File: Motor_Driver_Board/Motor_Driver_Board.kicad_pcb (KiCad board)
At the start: 2 copper layers, 74.5 x 55 mm, 9 parts, among them J1 Conn_01x02_MountingPin, J2 Conn_01x04_MountingPin

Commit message: Shcematic and layout
Updated the schematic.
Updated the layout.
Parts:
- removed REF** (x4): MountingHole_3.5mm, MountingHole:MountingHole_3.5mm
- added C2: 100u, Capacitor_THT:CP_Radial_D6.3mm_P2.50mm, F.Cu at (148.8, 60.6)
- added C3: 10u, Capacitor_SMD:C_1206_3216Metric, F.Cu at (144.3, 60.6)
- added C4: 47u, Capacitor_SMD:C_1206_3216Metric, F.Cu at (132.8, 63.6)
- added C5: 47u, Capacitor_SMD:C_1206_3216Metric, F.Cu at (132.8, 60.6)
- added C6: 47u, Capacitor_SMD:C_1206_3216Metric, F.Cu at (132.8, 57.6)
- added C7: 10n, Capacitor_SMD:C_0603_1608Metric, F.Cu at (188.5, 42.6)
- added C8: 10n, Capacitor_SMD:C_0603_1608Metric, F.Cu at (188.5, 45.1)
- added C9: 10n, Capacitor_SMD:C_0603_1608Metric, F.Cu at (188.5, 47.7)
- added D1: SS34, Diode_SMD:D_SMA, F.Cu at (148.8, 49.6)
- added H1: MH, MountingHole:MountingHole_3.2mm_M3, F.Cu at (67.3, 39.6)
- added H2: MH, MountingHole:MountingHole_3.2mm_M3, F.Cu at (157.3, 39.6)
- added H3: MH, MountingHole:MountingHole_3.2mm_M3, F.Cu at (67.3, 129.6)
- added H4: MH, MountingHole:MountingHole_3.2mm_M3, F.Cu at (157.3, 129.6)
- added J3: LCD, Connector_PinHeader_2.54mm:PinHeader_1x04_P2.54mm_Vertical, F.Cu at (190.3, 77.5)
- added L1: FXL1040-680-M, Inductor_SMD:L_Sunlord_MWSA1005S, F.Cu at (139.3, 49.6)
- added R1: 10K, Resistor_SMD:R_0603_1608Metric, F.Cu at (188.5, 50.2)
- added R10: 10K, Resistor_SMD:R_0603_1608Metric, F.Cu at (194.6, 76.4)
- added R11: 10K, Resistor_SMD:R_0603_1608Metric, F.Cu at (194.6, 79.0)
- added R2: 10K, Resistor_SMD:R_0603_1608Metric, F.Cu at (188.5, 52.7)
- added R3: 10K, Resistor_SMD:R_0603_1608Metric, F.Cu at (188.5, 55.2)
- added R4: 10K, Resistor_SMD:R_0603_1608Metric, F.Cu at (188.5, 57.7)
- added R5: 10K, Resistor_SMD:R_0603_1608Metric, F.Cu at (188.5, 60.2)
- added R6: 10K, Resistor_SMD:R_0603_1608Metric, F.Cu at (188.5, 62.7)
- added R7: 10K, Resistor_SMD:R_0603_1608Metric, F.Cu at (192.3, 101.1)
- added R8: 10K, Resistor_SMD:R_0603_1608Metric, F.Cu at (192.3, 103.6)
- added R9: 10K, Resistor_SMD:R_0603_1608Metric, F.Cu at (192.3, 106.1)
- added SW1: ENCODER, Rotary_Encoder:RotaryEncoder_Alps_EC11E-Switch_Vertical_H20mm_CircularMountingHoles, F.Cu at (192.6, 47.1)
- added U1: XL1509-5.0, Package_SO:SOIC-8_3.9x4.9mm_P1.27mm, F.Cu at (139.3, 60.6)
- A1: value Pololu_Breakout_A4988 -> A4988
- C1: value C_Polarized 100uF -> 100u; footprint Capacitor_THT:CP_Axial_L18.0mm_D8.0mm_P25.00mm_Horizontal -> Capacitor_THT:CP_Radial_D6.3mm_P2.50mm
- J1: value Conn_01x02_MountingPin -> POWER
- J2: value Conn_01x04_MountingPin -> MOTOR
- moved J2 120.4 mm to (69.8, 55.8), turned to 0 degrees
- moved A1 111.3 mm to (81.0, 50.7), turned to 0 degrees
- moved C1 91.0 mm to (79.8, 77.1)
- moved A2 48.6 mm to (112.3, 61.6), turned to 0 degrees
- moved J1 31.6 mm to (156.3, 54.6), turned to 180 degrees
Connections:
- net Net-(A1-1A) renamed /A1
- net Net-(A1-1B) renamed /B1
- net Net-(A1-DIR) renamed /STEP
- net Net-(A1-MS1) renamed /MS1
- net Net-(A1-MS2) renamed /MS2
- net Net-(A1-MS3) renamed /MS3
- net Net-(A1-STEP) renamed /DIR
- net Net-(A1-VMOT) renamed VCC
- net Net-(A1-~{RESET}) renamed /RST
- A1 pad 2: Net-(A1-VDD) -> +5V
- A1 pad 5: Net-(A1-2A) -> /A2
- A1 pad 6: Net-(A1-2B) -> /B2
- A2 pad 11: unconnected-(A2-GPIO8-Pad11)_1 -> /SDA
- A2 pad 12: unconnected-(A2-GPIO9-Pad12) -> /SCL
- A2 pad 15: unconnected-(A2-GPIO11-Pad15)_1 -> /ENC_CW
- A2 pad 17: unconnected-(A2-GPIO13-Pad17) -> /ENC_CC
- A2 pad 20: unconnected-(A2-GPIO15-Pad20)_1 -> /ENC_SW
- A2 pad 33: GND -> unconnected-(A2-AGND-Pad33)_1
- A2 pad 36: unconnected-(A2-3V3-Pad36)_1 -> +3V3
- A2 pad 39: unconnected-(A2-VSYS-Pad39) -> +5V
- A2 pad 40: Net-(A1-VDD) -> unconnected-(A2-VBUS-Pad40)
- J2 pad 3: Net-(A1-2A) -> /B2
- J2 pad 4: Net-(A1-2B) -> /A2
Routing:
- net Net-(A1-VDD): track 51.3 -> 0.00 mm
- net VCC: track 35.3 -> 13.9 mm
- net +5V: track 0.00 -> 16.5 mm
- net /MS1: track 11.5 -> 0.00 mm
- net /MS2: track 11.5 -> 0.00 mm
- net /MS3: track 11.5 -> 0.00 mm
- net Net-(A1-2B): track 10.5 -> 0.00 mm
- net Net-(A1-2A): track 10.5 -> 0.00 mm
- net /B1: track 10.5 -> 0.00 mm
- net /A1: track 10.5 -> 0.00 mm
- net /STEP: track 10.4 -> 0.00 mm
- net /DIR: track 10.4 -> 0.00 mm
- net /RST: track 2.54 -> 0.00 mm
- added copper zone on F.Cu, net +5V
- added copper zone on F.Cu, net /DC_OUT
- added copper zone on F.Cu, net GND
- added copper zone on F.Cu, net VCC
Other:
- board size 74.5 x 55 mm -> 100 x 100 mm
- board text removed: "100uF"
- board text removed: "1A"
- board text removed: "1B"
- board text removed: "2A"
- board text removed: "2B"
- board text removed: "A4988 Stepper Motor Driver Control Board RW"
- board text removed: "DIR"
- board text removed: "MS1"
- board text removed: "MS2"
- board text removed: "MS3"
- board text removed: "STEP"
- board text removed: "VIN (8-35V)"

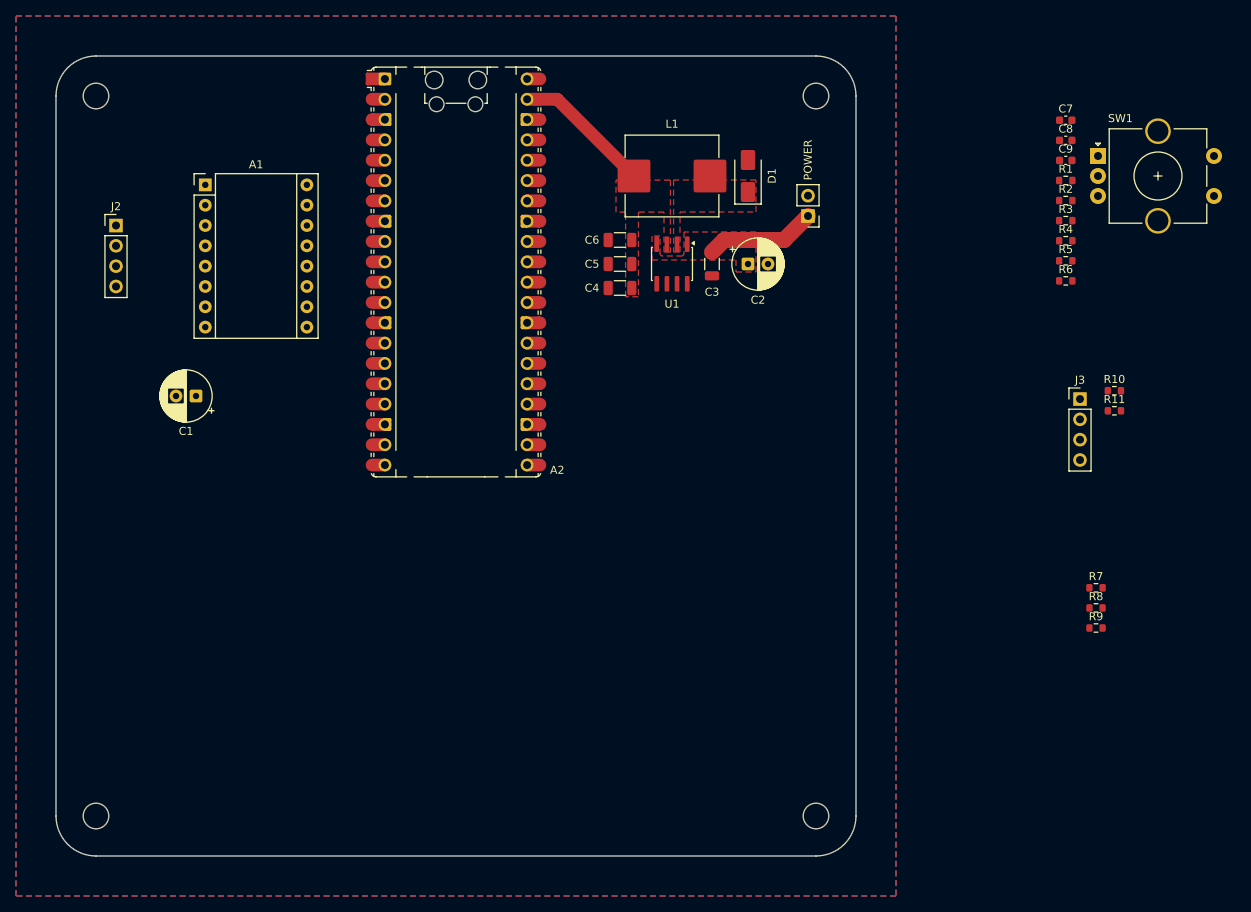
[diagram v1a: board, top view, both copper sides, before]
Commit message: Switch to RP2040-Zero
Switched controller to RP2040-Zero to save space, schematic updated.
PCB layout in progress
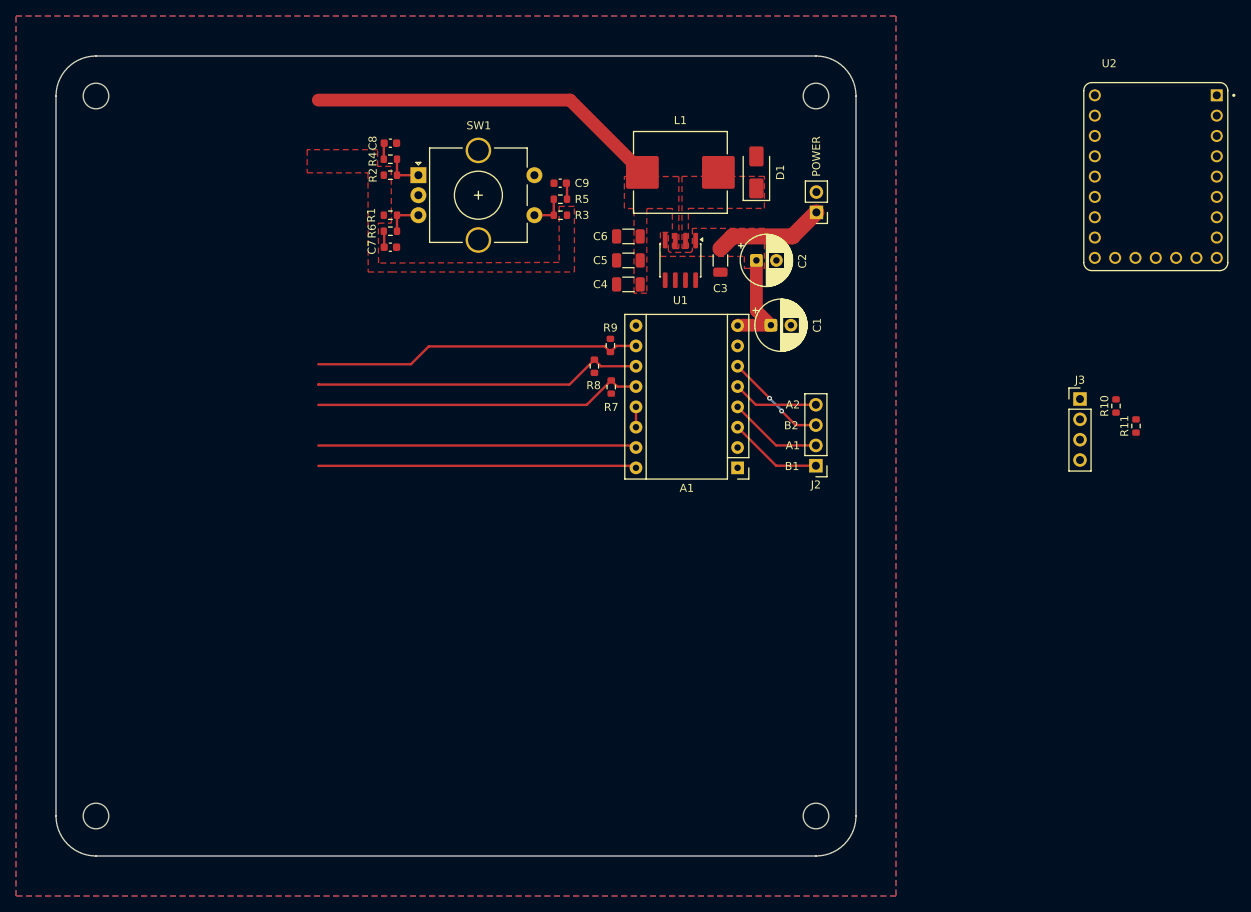
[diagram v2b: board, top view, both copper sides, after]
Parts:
- removed A2: RaspberryPi_Pico, Module:RaspberryPi_Pico_Common_Unspecified
- added U2: ~, RP2040Zero:MODULE_RP2040-ZERO, F.Cu at (199.8, 49.7)
- moved J2 92.5 mm to (157.3, 85.8), turned to 180 degrees
- moved C7 85.9 mm to (104.1, 58.5)
- moved R4 85.0 mm to (104.1, 47.5), turned to 180 degrees
- moved SW1 85.0 mm to (107.6, 49.5)
- moved R6 84.6 mm to (104.1, 56.5), turned to 180 degrees
- moved R1 84.5 mm to (104.1, 54.5)
- moved R2 84.5 mm to (104.1, 49.5)
- moved C8 84.4 mm to (104.1, 45.5)
- moved A1 75.4 mm to (147.5, 86.1), turned to 180 degrees
- moved C1 72.4 mm to (151.7, 68.3), turned to 0 degrees
- moved R9 70.2 mm to (131.6, 70.8), turned to 90 degrees
- moved R8 69.6 mm to (129.6, 73.4), turned to -90 degrees
- moved R7 65.6 mm to (131.7, 76.0), turned to -90 degrees
- moved R5 63.6 mm to (125.4, 52.5), turned to 180 degrees
- moved C9 63.3 mm to (125.3, 50.5), turned to 180 degrees
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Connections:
- A1 pad 15: /DIR -> /STEP
- A1 pad 16: /STEP -> /DIR
- R7 pad 1: /MS1 -> /MS3
- R9 pad 1: /MS3 -> /MS1
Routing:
- net /MS2: track 0.00 -> 41.5 mm
- net /MS3: track 0.00 -> 41.4 mm
- net /MS1: track 0.00 -> 41.3 mm
- net /STEP: track 0.00 -> 39.8 mm
- net /DIR: track 0.00 -> 39.8 mm
- net +5V: track 16.5 -> 44.3 mm
- net VCC: track 13.9 -> 27.0 mm
- net /B2: track 0.00 -> 12.9 mm, vias 0 -> 2
- net /A1: track 0.00 -> 11.8 mm
- net /B1: track 0.00 -> 11.8 mm
- net /A2: track 0.00 -> 10.7 mm
- net Net-(R1-Pad2): track 0.00 -> 4.77 mm
- net Net-(R2-Pad2): track 0.00 -> 4.67 mm
- net Net-(R3-Pad2): track 0.00 -> 4.42 mm
- net /RST: track 0.00 -> 2.54 mm
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- added copper zone on F.Cu, net +3V3
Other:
- board text added: "A1"
- board text added: "A2"
- board text added: "B1"
- board text added: "B2"

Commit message: Added RP2040-Zero Microcontroller
Switched previous Pi Pico to RP2040-Zero by Waveshare to reduce overall board size. Layout complete, via hatching still required
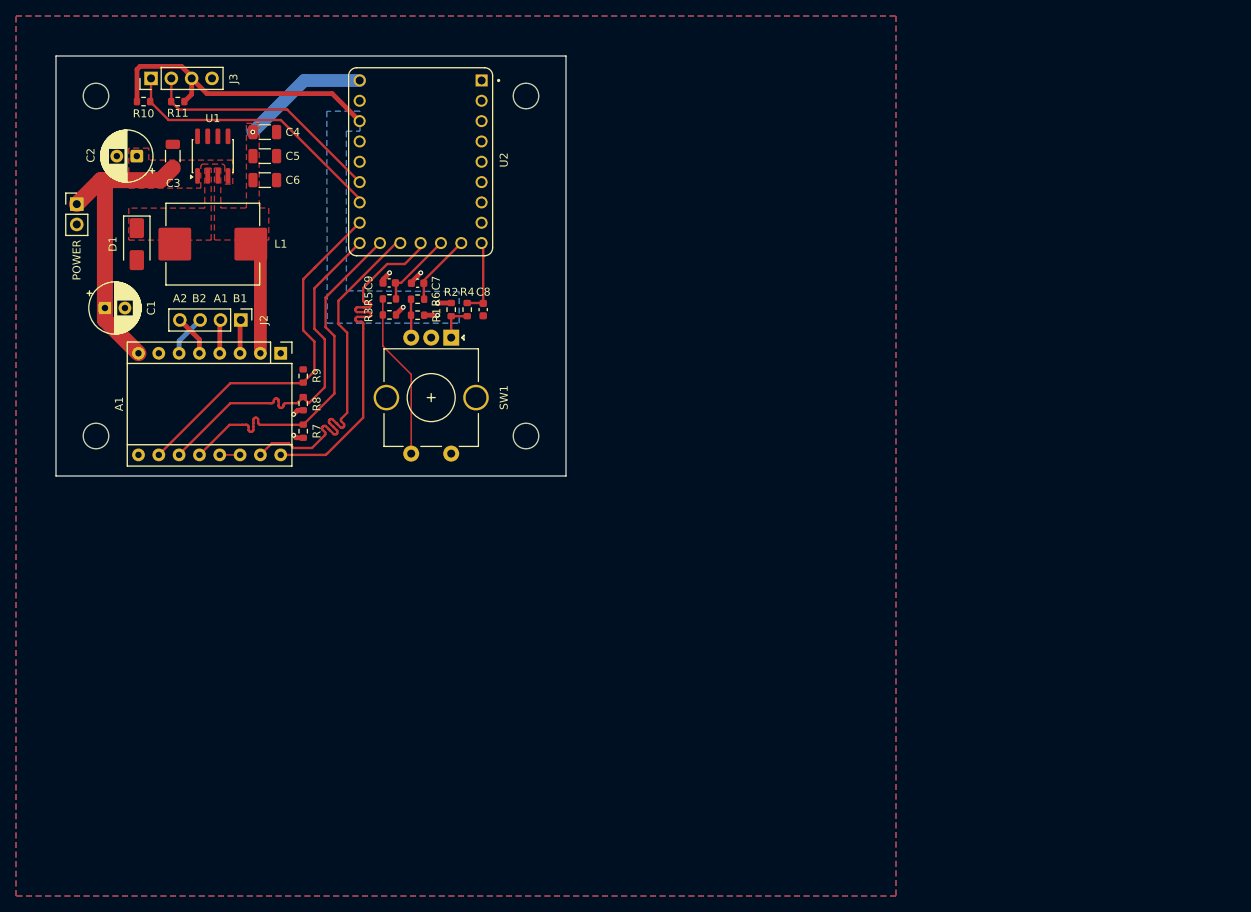
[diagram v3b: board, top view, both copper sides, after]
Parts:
- moved R10 127.4 mm to (73.3, 40.3), turned to 0 degrees
- moved R11 126.5 mm to (77.5, 40.3), turned to 180 degrees
- moved J3 122.8 mm to (74.2, 37.4), turned to 90 degrees
- moved J1 92.5 mm to (64.9, 53.1), turned to 0 degrees
- moved U2 91.9 mm to (107.9, 47.8)
- moved C1 83.3 mm to (68.4, 66.1)
- moved C2 78.5 mm to (72.4, 47.1), turned to 180 degrees
- moved D1 78.0 mm to (72.4, 58.1), turned to -90 degrees
- moved J2 74.2 mm to (85.4, 67.6), turned to -90 degrees
- moved C3 69.7 mm to (76.9, 47.1), turned to 90 degrees
- moved U1 59.9 mm to (81.9, 47.1), turned to 90 degrees
- moved H4 59.8 mm to (121.1, 82.1)
- moved L1 59.1 mm to (81.9, 58.1), turned to 0 degrees
- moved A1 58.9 mm to (90.4, 71.8), turned to -90 degrees
- moved C4 49.3 mm to (88.4, 44.1), turned to 0 degrees
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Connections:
- U2 pad 1: /ENC_CC -> unconnected-(U2-GPIO_0-Pad1)
- U2 pad 10: unconnected-(U2-GPIO_9-Pad10) -> /ENC_CW
- U2 pad 11: /SDA -> /ENC_SW
- U2 pad 12: /SCL -> /DIR
- U2 pad 13: unconnected-(U2-GPIO_12-Pad13) -> /STEP
- U2 pad 14: unconnected-(U2-GPIO_13-Pad14) -> /MS3
- U2 pad 15: unconnected-(U2-GPIO_14-Pad15) -> /MS2
- U2 pad 16: unconnected-(U2-GPIO_15-Pad16) -> /MS1
- U2 pad 17: unconnected-(U2-GPIO_26-Pad17) -> /SDA
- U2 pad 18: unconnected-(U2-GPIO_27-Pad18) -> /SCL
- U2 pad 2: /ENC_CW -> unconnected-(U2-GPIO_1-Pad2)
- U2 pad 3: /ENC_SW -> unconnected-(U2-GPIO_2-Pad3)
- U2 pad 5: /MS3 -> unconnected-(U2-GPIO_4-Pad5)
- U2 pad 6: /MS2 -> unconnected-(U2-GPIO_5-Pad6)
- U2 pad 7: /MS1 -> unconnected-(U2-GPIO_6-Pad7)
- U2 pad 8: /DIR -> unconnected-(U2-GPIO_7-Pad8)
- U2 pad 9: /STEP -> /ENC_CC
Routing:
- net +3V3: track 0.00 -> 43.0 mm, vias 0 -> 3
- net /SDA: track 0.00 -> 34.6 mm
- net /SCL: track 0.00 -> 30.6 mm
- net Net-(R3-Pad2): track 4.42 -> 20.8 mm
- net +5V: track 44.3 -> 30.2 mm, vias 0 -> 1
- net VCC: track 27.0 -> 37.5 mm
- net /ENC_SW: track 2.03 -> 9.68 mm
- net /B2: track 12.9 -> 5.25 mm, vias 2 -> 0
- net /ENC_CC: track 2.02 -> 9.65 mm
- net /A1: track 11.8 -> 4.20 mm
- net /B1: track 11.8 -> 4.20 mm
- net /ENC_CW: track 2.12 -> 9.08 mm
- net GND: track 0.00 -> 6.14 mm, vias 0 -> 4
- net /A2: track 10.7 -> 5.17 mm
- net /STEP: track 39.8 -> 45.0 mm
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- added copper zone on B.Cu, net +3V3
- removed copper zone on F.Cu, net +3V3
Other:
- board size 100 x 100 mm -> 63.8 x 52.5 mm
